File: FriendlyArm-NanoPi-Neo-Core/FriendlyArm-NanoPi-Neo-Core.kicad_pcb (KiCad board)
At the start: 2 copper layers, 41.9 x 41.5 mm, 11 parts, among them J1 Conn_02x12_Odd_Even, J2 Conn_02x12_Odd_Even, J3 Conn_02x10_Odd_Even

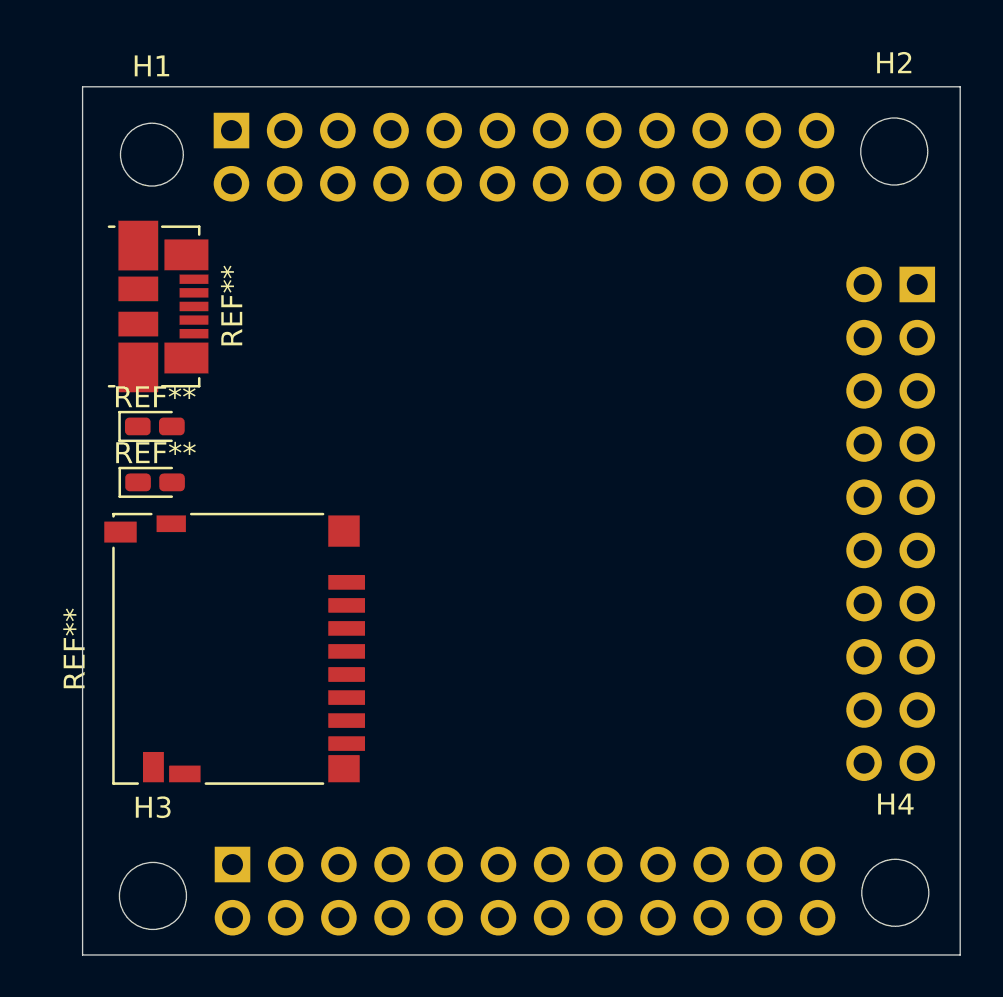
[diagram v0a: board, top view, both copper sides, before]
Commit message: nanopi neo core: "finished" model
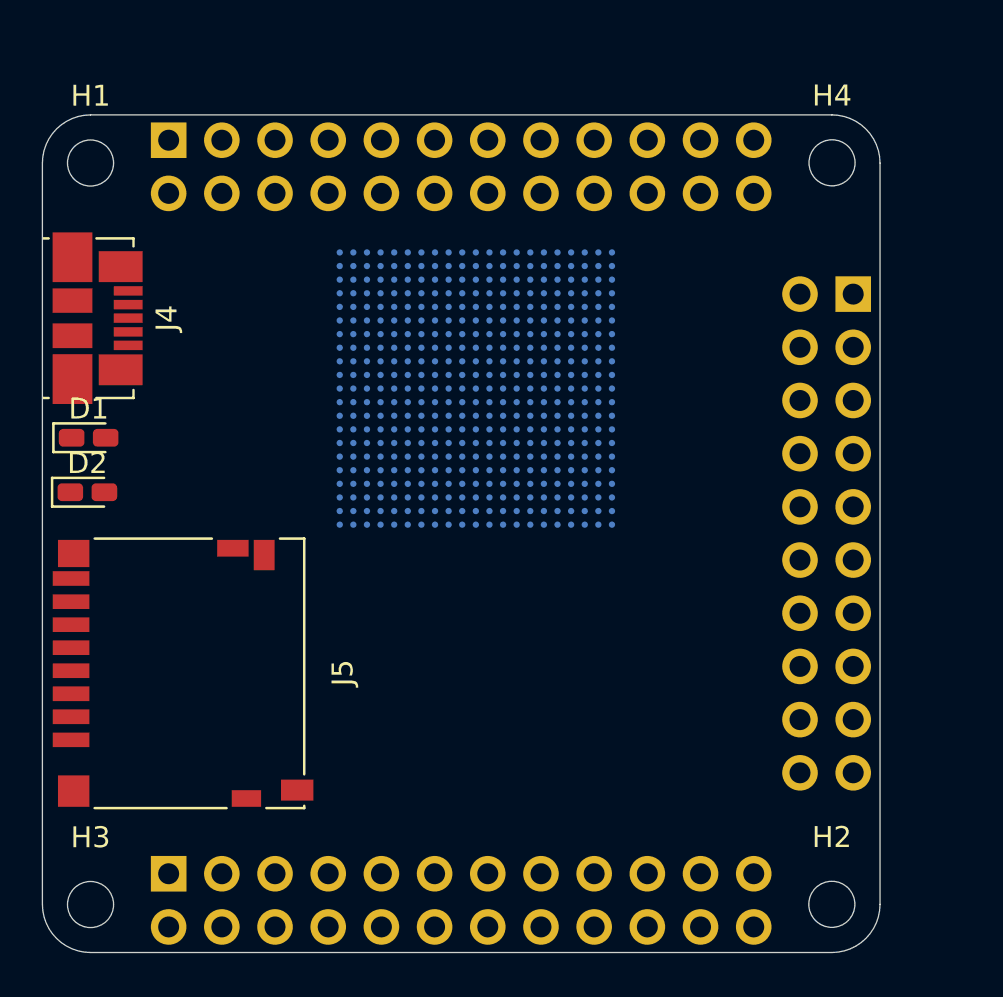
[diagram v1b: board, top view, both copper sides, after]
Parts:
- removed the REF** at (30.4, 34.0)
- removed the REF** at (33.8, 50.4)
- removed the REF** at (30.0, 39.8)
- removed the REF** at (30.0, 42.5)
- added D1: LED, LED_SMD:LED_0603_1608Metric_Castellated, F.Cu at (26.8, 40.3)
- added D2: LED, LED_SMD:LED_0603_1608Metric_Castellated, F.Cu at (26.8, 42.9)
- added J4: USB_OTG, Connector_USB:USB_Micro-B_Molex_47346-0001, F.Cu at (27.3, 34.6)
- added J5: Micro_SD_Card, Connector_Card:microSD_HC_Hirose_DM3D-SF, F.Cu at (31.3, 51.6)
- added REF**: BGA-347_21x21_14.0x14.0mm, Package_BGA:BGA-347_21x21_14.0x14.0mm, B.Cu at (45.3, 38.0)
- H1, H2, H3, H4: footprint MountingHole:MountingHole_3.2mm_M3 -> MountingHole:MountingHole_2.2mm_M2
- moved H2 36.1 mm to (62.3, 62.6)
- moved H4 35.0 mm to (62.3, 27.2)
- moved J3 3.09 mm to (63.3, 33.5)
- moved J1 3.08 mm to (30.6, 61.1)
- moved J2 3.04 mm to (30.6, 26.1)
- moved H3 3.01 mm to (26.9, 62.6)
- moved H1 2.96 mm to (26.9, 27.2)
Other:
- board size 41.9 x 41.5 mm -> 40 x 40 mm

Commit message: nanopi core: update to kicad 5.99x project files
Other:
- net class Default removed

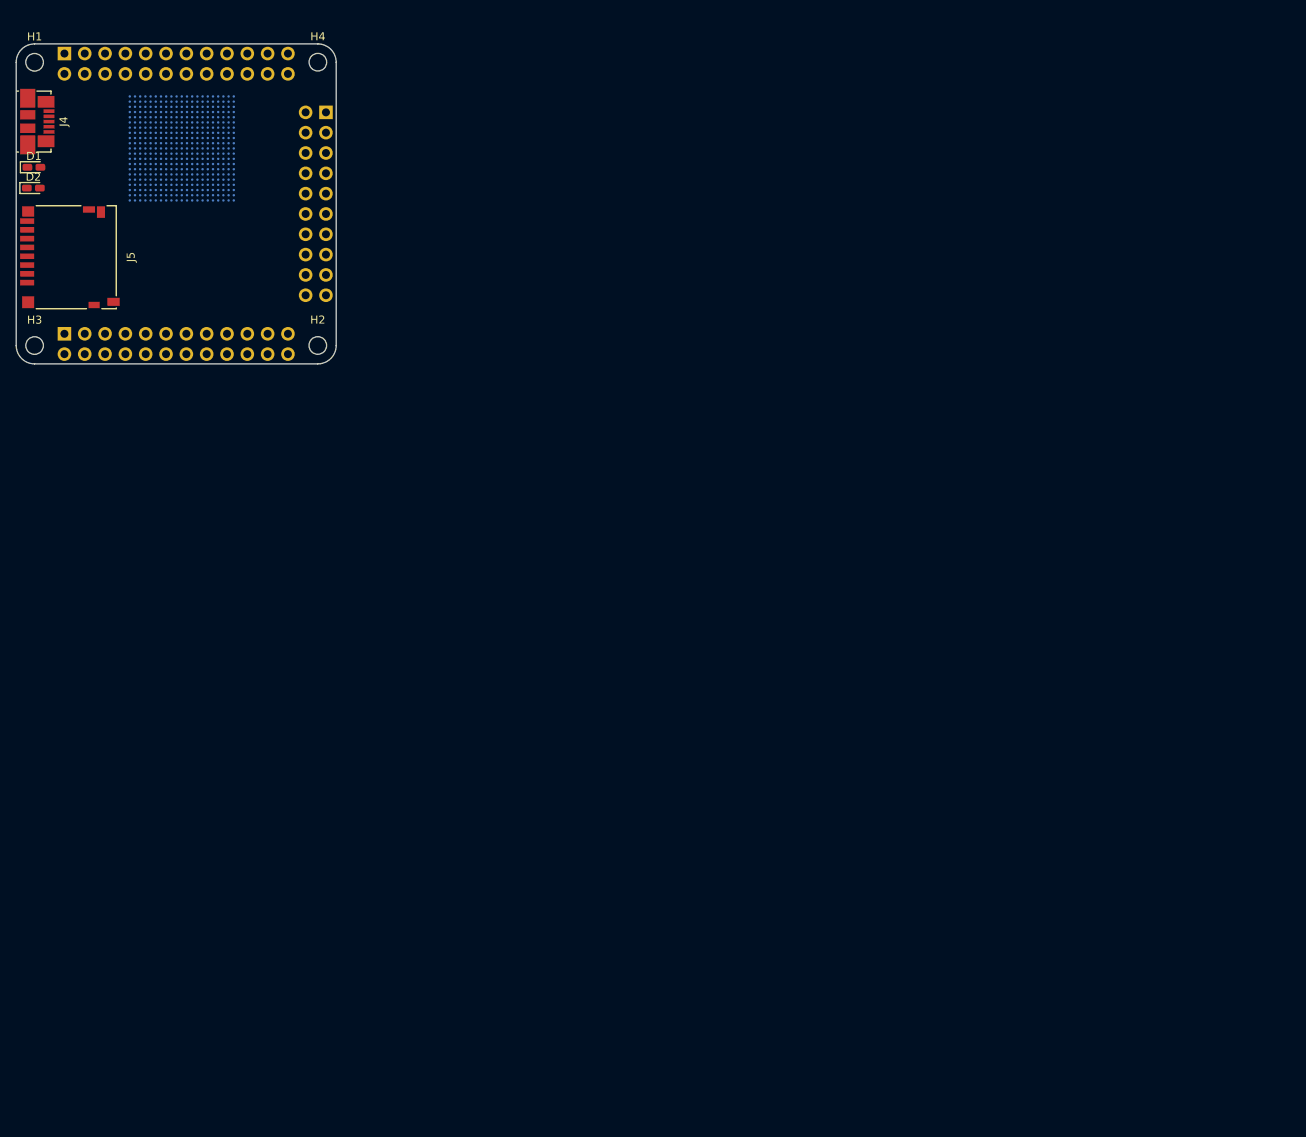
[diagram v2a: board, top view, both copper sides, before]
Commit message: nanopi-core: completely overhaul model
Properly numerically align, place all big bgas, label headers
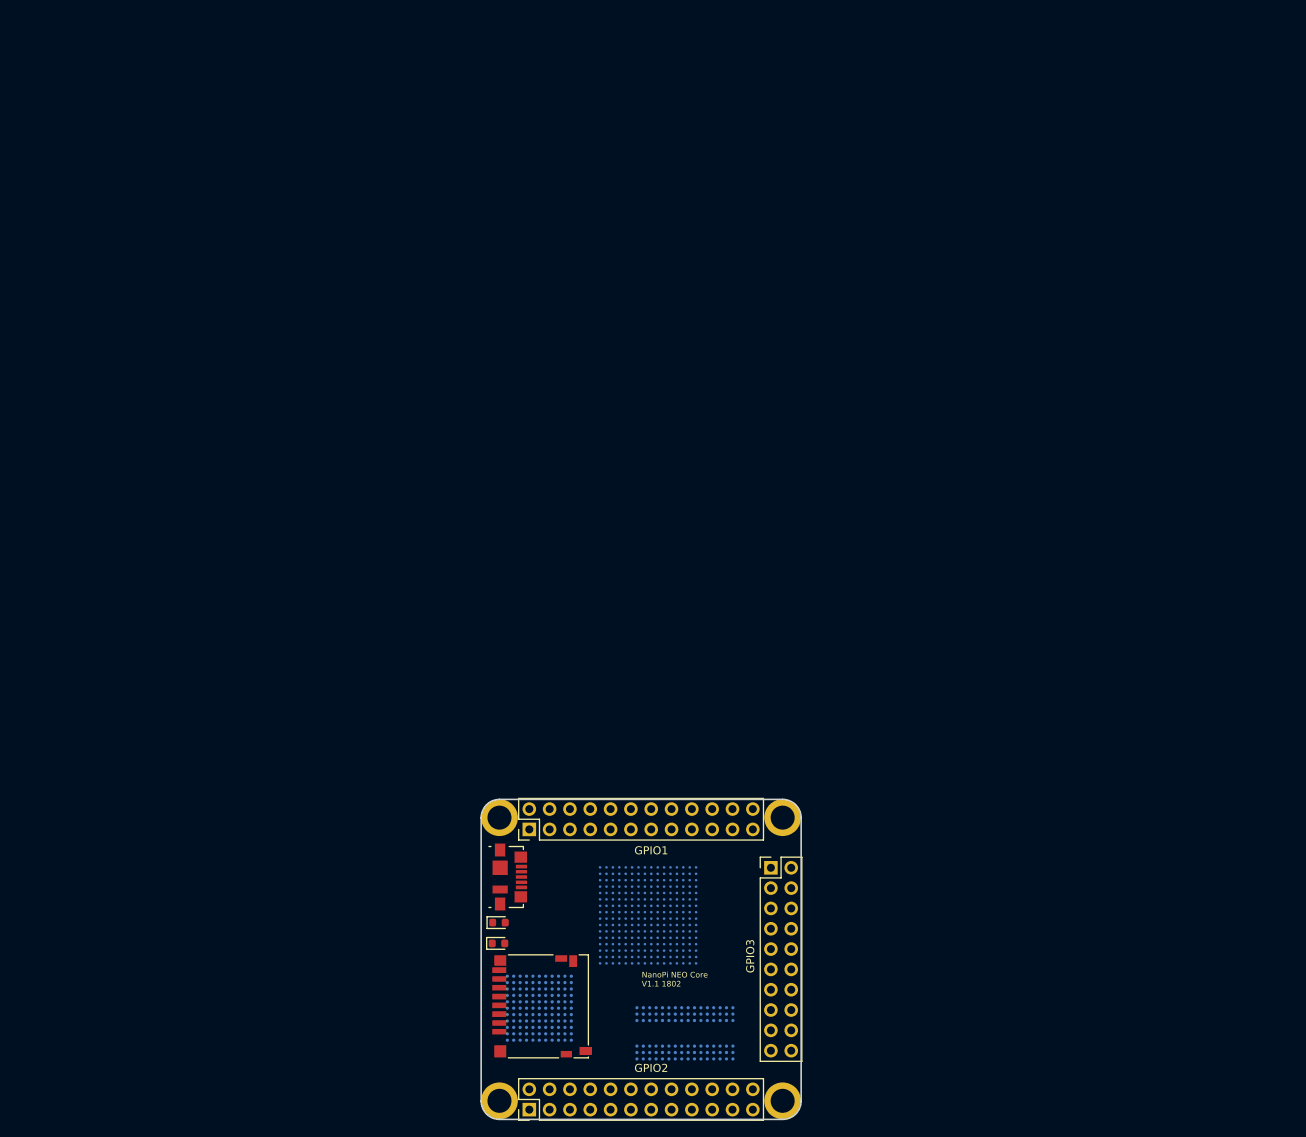
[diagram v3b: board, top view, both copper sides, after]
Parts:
- removed the REF** at (45.3, 38.0)
- added REF**: BGA-96_9.0x13.0mm_Layout2x3x16_P0.8mm, Package_BGA:BGA-96_9.0x13.0mm_Layout2x3x16_P0.8mm, B.Cu at (108.2, 148.6)
- added REF**: BGA-256_14.0x14.0mm_Layout16x16_P0.8mm_Ball0.45mm_Pad0.32mm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, Package_BGA:BGA-256_14.0x14.0mm_Layout16x16_P0.8mm_Ball0.45mm_Pad0.32mm_NSMD, B.Cu at (103.6, 133.8)
- added REF**: TFBGA-121_10x10mm_Layout11x11_P0.8mm, Package_BGA:TFBGA-121_10x10mm_Layout11x11_P0.8mm, B.Cu at (90.0, 145.4)
- D1, D2: footprint LED_SMD:LED_0603_1608Metric_Castellated -> LED_SMD:LED_0603_1608Metric
- H1, H2, H3, H4: footprint MountingHole:MountingHole_2.2mm_M2 -> MountingHole:MountingHole_3mm_Pad
- J1, J2, J3: moved to F.Cu
- moved J2 144.2 mm to (88.8, 158.1), turned to 90 degrees
- moved H3 132.9 mm to (120.4, 157.0)
- moved D1 113.1 mm to (84.9, 137.3)
- moved J4 111.4 mm to (86.3, 129.0)
- moved H4 110.9 mm to (120.4, 121.6)
- moved H1 110.9 mm to (85.0, 121.6)
- moved J5 110.7 mm to (90.4, 145.2)
- moved J3 109.6 mm to (119.0, 127.9), turned to 0 degrees
- moved D2 108.7 mm to (85.0, 134.7)
- moved H2 97.1 mm to (85.0, 157.0)
- moved J1 84.9 mm to (88.8, 123.1), turned to 90 degrees
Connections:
- H1 pad 1: (no net) -> unconnected-(H1-Pad1)
- H2 pad 1: (no net) -> unconnected-(H2-Pad1)
- H3 pad 1: (no net) -> unconnected-(H3-Pad1)
- H4 pad 1: (no net) -> unconnected-(H4-Pad1)
- J4 pad 6: Net-(J4-Pad6) -> unconnected-(J4-Pad6)
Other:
- board text added: "3V3"
- board text added: "5V"
- board text added: "A"
- board text added: "BCK"
- board text added: "CD"
- board text added: "CD/DAT3"
- board text added: "CLK"
- board text added: "CLK0"
- board text added: "CLK1"
- board text added: "CMD"
- board text added: "CS0"
- board text added: "CS1"
- board text added: "DAT0"
- board text added: "DAT1"
- board text added: "DAT2"
- board text added: "DM1"
- board text added: "DM2"
- board text added: "DM3"
- board text added: "DP1"
- board text added: "DP2"
- board text added: "DP3"
- board text added: "FRIENDLY ELEC"
- board text added: "G"
- board text added: "GND"
- board text added: "GPIO1"
- board text added: "GPIO2"
- board text added: "GPIO3"
- board text added: "IOA2"
- board text added: "IOA3"
- board text added: "IOA6"
- board text added: "IOA7"
- board text added: "IOG11"
- board text added: "IOG8"
- board text added: "IOG9"
- board text added: "IRRX"
- board text added: "LL"
- board text added: "LNK"
- board text added: "LR"
- board text added: "LRCK"
- board text added: "MISO0"
- board text added: "MISO1"
- board text added: "MN"
- board text added: "MOSI0"
- board text added: "MOSI1"
- board text added: "MP"
- board text added: "NC"
- board text added: "NanoPi NEO Core"
- board text added: "NanoPi NEO Core V1.1 1802"
- board text added: "RX0"
- board text added: "RX1"
- board text added: "RX2"
- board text added: "RXN"
- board text added: "RXP"
- board text added: "SCL0"
- board text added: "SCL2"
- board text added: "SDA0"
- board text added: "SDA2"
- board text added: "SDIN"
- board text added: "SDOT"
- board text added: "SPD"
- board text added: "SPDF"
- board text added: "TX0"
- board text added: "TX1"
- board text added: "TX2"
- board text added: "TXN"
- board text added: "TXP"
- board text added: "V1.1 1802"
- board text added: "VDD"
- board text added: "VSS"

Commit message: nano-pi neo core: fix emmc, add parts on edge
There's a fairly high sot23 part rigth on the edge that you may want to
be careful with if you're cramming things....

Also, this uses a proper model for the emmc that is positioned better
and has the right heights.
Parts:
- removed REF**: BGA-96_9.0x13.0mm_Layout2x3x16_P0.8mm, Package_BGA:BGA-96_9.0x13.0mm_Layout2x3x16_P0.8mm
- removed REF**: BGA-256_14.0x14.0mm_Layout16x16_P0.8mm_Ball0.45mm_Pad0.32mm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, Package_BGA:BGA-256_14.0x14.0mm_Layout16x16_P0.8mm_Ball0.45mm_Pad0.32mm_NSMD
- removed REF**: TFBGA-121_10x10mm_Layout11x11_P0.8mm, Package_BGA:TFBGA-121_10x10mm_Layout11x11_P0.8mm
- added IC1: Memory_eMMC_Samsung-KLM8G1WEMB-B031, et-parts:BGA153_P0.5mm_14X14_11.5x13.0mm_h0.8mm_Samsung_eMMC, B.Cu at (150.5, 117.7)
- added N1: Housing, Package_BGA:BGA-256_14.0x14.0mm_Layout16x16_P0.8mm_Ball0.45mm_Pad0.32mm_NSMD, B.Cu at (164.5, 106.3)
- added Q1: AO3401A, Package_TO_SOT_SMD:SOT-23, B.Cu at (145.9, 108.5)
- added Q2: BC856BS, Package_TO_SOT_SMD:SOT-363_SC-70-6, B.Cu at (146.6, 101.7)
- added U1: AS4C256M16D3, Package_BGA:BGA-96_9.0x13.0mm_Layout2x3x16_P0.8mm, B.Cu at (169.1, 121.0)
- moved D2 66.9 mm to (145.8, 107.1)
- moved J5 66.9 mm to (151.2, 117.6)
- moved D1 66.9 mm to (145.8, 109.7)
- moved H1 66.9 mm to (145.9, 94.0)
- moved H2 66.9 mm to (145.9, 129.4)
- moved H3 66.9 mm to (181.3, 129.4)
- moved H4 66.9 mm to (181.3, 94.0)
- moved J3 66.9 mm to (179.8, 100.3)
- moved J4 66.9 mm to (147.2, 101.4)
- moved J1 66.9 mm to (149.6, 95.5)
- moved J2 66.9 mm to (149.6, 130.5)
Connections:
- D1 pad 1: (no net) -> unconnected-(D1-Pad1)
- D1 pad 2: (no net) -> unconnected-(D1-Pad2)
- D2 pad 1: (no net) -> unconnected-(D2-Pad1)
- D2 pad 2: (no net) -> unconnected-(D2-Pad2)
- J1 pad 1: (no net) -> unconnected-(J1-Pad1)
- J1 pad 10: (no net) -> unconnected-(J1-Pad10)
- J1 pad 11: (no net) -> unconnected-(J1-Pad11)
- J1 pad 12: (no net) -> unconnected-(J1-Pad12)
- J1 pad 13: (no net) -> unconnected-(J1-Pad13)
- J1 pad 14: (no net) -> unconnected-(J1-Pad14)
- J1 pad 15: (no net) -> unconnected-(J1-Pad15)
- J1 pad 16: (no net) -> unconnected-(J1-Pad16)
- J1 pad 17: (no net) -> unconnected-(J1-Pad17)
- J1 pad 18: (no net) -> unconnected-(J1-Pad18)
- J1 pad 19: (no net) -> unconnected-(J1-Pad19)
- J1 pad 2: (no net) -> unconnected-(J1-Pad2)
- J1 pad 20: (no net) -> unconnected-(J1-Pad20)
- J1 pad 21: (no net) -> unconnected-(J1-Pad21)
- J1 pad 22: (no net) -> unconnected-(J1-Pad22)
- J1 pad 23: (no net) -> unconnected-(J1-Pad23)
- J1 pad 24: (no net) -> unconnected-(J1-Pad24)
- J1 pad 3: (no net) -> unconnected-(J1-Pad3)
- J1 pad 4: (no net) -> unconnected-(J1-Pad4)
- J1 pad 5: (no net) -> unconnected-(J1-Pad5)
- J1 pad 6: (no net) -> unconnected-(J1-Pad6)
- J1 pad 7: (no net) -> unconnected-(J1-Pad7)
- J1 pad 8: (no net) -> unconnected-(J1-Pad8)
- J1 pad 9: (no net) -> unconnected-(J1-Pad9)
- J2 pad 1: (no net) -> unconnected-(J2-Pad1)
- J2 pad 10: (no net) -> unconnected-(J2-Pad10)
- J2 pad 11: (no net) -> unconnected-(J2-Pad11)
- J2 pad 12: (no net) -> unconnected-(J2-Pad12)
- J2 pad 13: (no net) -> unconnected-(J2-Pad13)
- J2 pad 14: (no net) -> unconnected-(J2-Pad14)
- J2 pad 15: (no net) -> unconnected-(J2-Pad15)
- J2 pad 16: (no net) -> unconnected-(J2-Pad16)
- J2 pad 17: (no net) -> unconnected-(J2-Pad17)
- J2 pad 18: (no net) -> unconnected-(J2-Pad18)
- J2 pad 19: (no net) -> unconnected-(J2-Pad19)
- J2 pad 2: (no net) -> unconnected-(J2-Pad2)
- J2 pad 20: (no net) -> unconnected-(J2-Pad20)
- J2 pad 21: (no net) -> unconnected-(J2-Pad21)
- J2 pad 22: (no net) -> unconnected-(J2-Pad22)
- J2 pad 23: (no net) -> unconnected-(J2-Pad23)
- J2 pad 24: (no net) -> unconnected-(J2-Pad24)
- J2 pad 3: (no net) -> unconnected-(J2-Pad3)
- J2 pad 4: (no net) -> unconnected-(J2-Pad4)
- J2 pad 5: (no net) -> unconnected-(J2-Pad5)
- J2 pad 6: (no net) -> unconnected-(J2-Pad6)
- J2 pad 7: (no net) -> unconnected-(J2-Pad7)
- J2 pad 8: (no net) -> unconnected-(J2-Pad8)
- J2 pad 9: (no net) -> unconnected-(J2-Pad9)
- J3 pad 1: (no net) -> unconnected-(J3-Pad1)
- J3 pad 10: (no net) -> unconnected-(J3-Pad10)
- J3 pad 11: (no net) -> unconnected-(J3-Pad11)
- J3 pad 12: (no net) -> unconnected-(J3-Pad12)
- J3 pad 13: (no net) -> unconnected-(J3-Pad13)
- J3 pad 14: (no net) -> unconnected-(J3-Pad14)
- J3 pad 15: (no net) -> unconnected-(J3-Pad15)
- J3 pad 16: (no net) -> unconnected-(J3-Pad16)
- J3 pad 17: (no net) -> unconnected-(J3-Pad17)
- J3 pad 18: (no net) -> unconnected-(J3-Pad18)
- J3 pad 19: (no net) -> unconnected-(J3-Pad19)
- J3 pad 2: (no net) -> unconnected-(J3-Pad2)
- J3 pad 20: (no net) -> unconnected-(J3-Pad20)
- J3 pad 3: (no net) -> unconnected-(J3-Pad3)
- J3 pad 4: (no net) -> unconnected-(J3-Pad4)
- J3 pad 5: (no net) -> unconnected-(J3-Pad5)
- J3 pad 6: (no net) -> unconnected-(J3-Pad6)
- J3 pad 7: (no net) -> unconnected-(J3-Pad7)
- J3 pad 8: (no net) -> unconnected-(J3-Pad8)
- J3 pad 9: (no net) -> unconnected-(J3-Pad9)
- J4 pad 1: (no net) -> unconnected-(J4-Pad1)
- J4 pad 2: (no net) -> unconnected-(J4-Pad2)
- J4 pad 3: (no net) -> unconnected-(J4-Pad3)
- J4 pad 4: (no net) -> unconnected-(J4-Pad4)
- J4 pad 5: (no net) -> unconnected-(J4-Pad5)
- J5 pad 1: (no net) -> unconnected-(J5-Pad1)
- J5 pad 2: (no net) -> unconnected-(J5-Pad2)
- J5 pad 3: (no net) -> unconnected-(J5-Pad3)
- J5 pad 4: (no net) -> unconnected-(J5-Pad4)
- J5 pad 5: (no net) -> unconnected-(J5-Pad5)
- J5 pad 6: (no net) -> unconnected-(J5-Pad6)
- J5 pad 7: (no net) -> unconnected-(J5-Pad7)
- J5 pad 8: (no net) -> unconnected-(J5-Pad8)
- J5 pad 9: (no net) -> unconnected-(J5-Pad9)
